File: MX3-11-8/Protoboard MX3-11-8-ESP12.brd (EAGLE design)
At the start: 74.4 x 99.4 mm, 638 parts, among them J1 DCJ0202, X1 ESP-12E, X3 RJ45

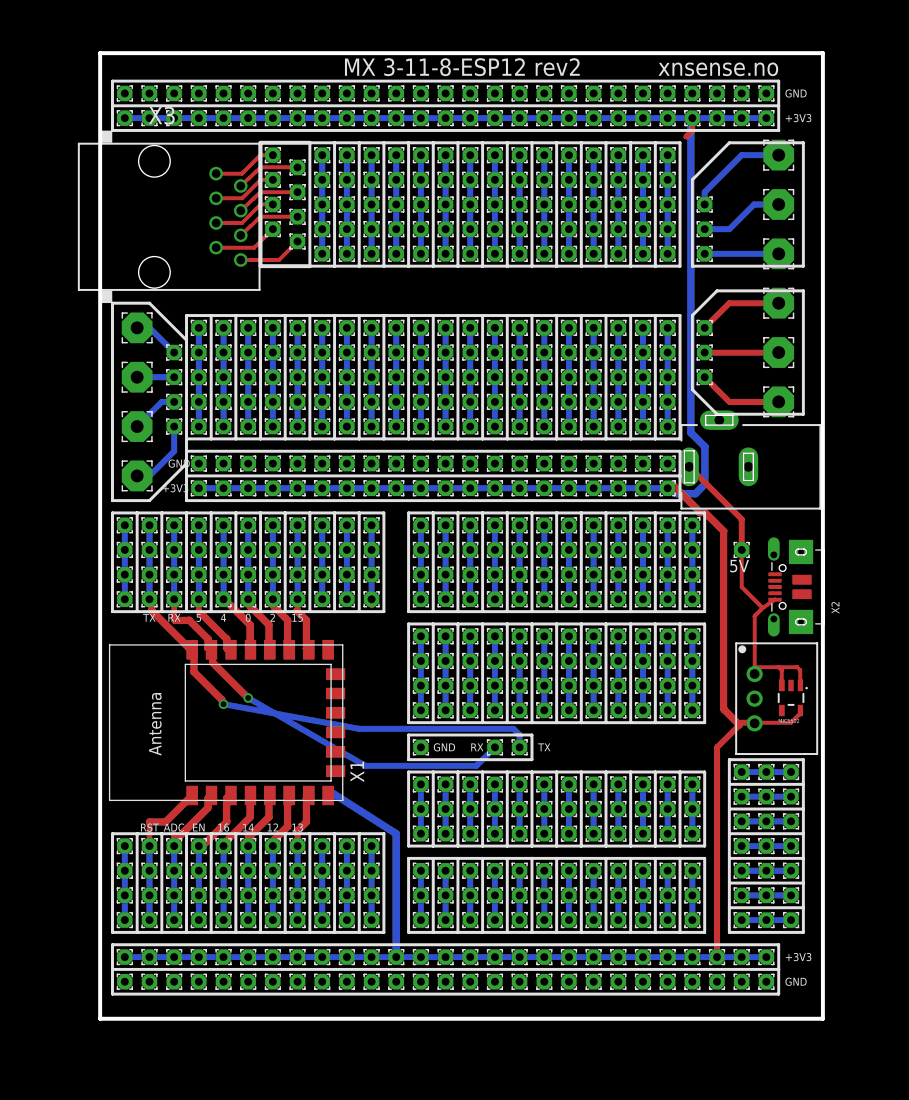
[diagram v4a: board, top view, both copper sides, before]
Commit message: Routed and Gerb files
Routed and produced gerb files
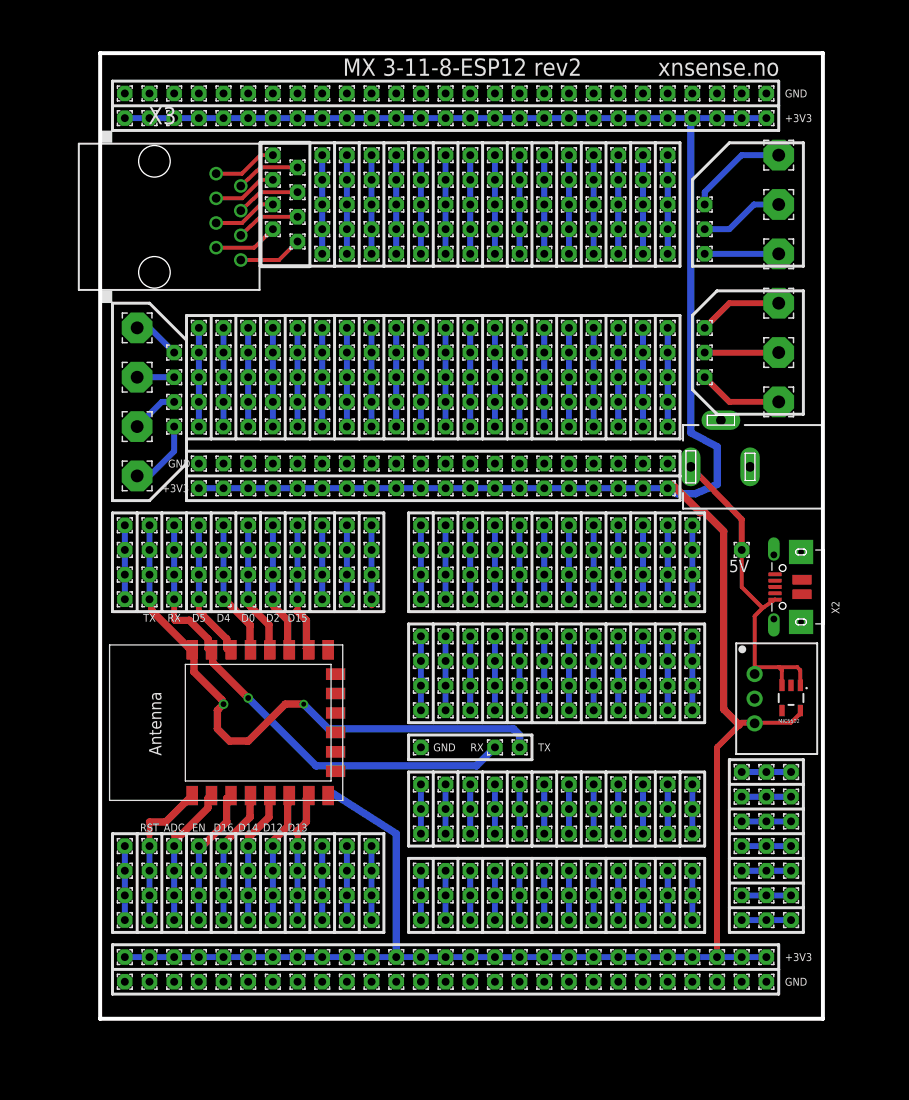
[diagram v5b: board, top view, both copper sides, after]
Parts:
- moved J1 0.16 mm to (63.9, 56.8)
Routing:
- net TX: track 54.5 -> 60.9 mm, vias 1 -> 2
- net RX: track 50.3 -> 51.3 mm
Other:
- board text added: "D0"
- board text added: "D12"
- board text added: "D13"
- board text added: "D14"
- board text added: "D15"
- board text added: "D16"
- board text added: "D2"
- board text added: "D4"
- board text added: "D5"
- board text removed: "0"
- board text removed: "12"
- board text removed: "13"
- board text removed: "14"
- board text removed: "15"
- board text removed: "16"
- board text removed: "2"
- board text removed: "4"
- board text removed: "5"
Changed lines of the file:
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@@
 <text x="7.62" y="19.685" size="0.8128" layer="25" align="center">ADC</text>
 <text x="10.16" y="19.685" size="0.8128" layer="25" align="center">EN</text>
-<text x="12.7" y="19.685" size="0.8128" layer="25" align="center">16</text>
-<text x="15.24" y="19.685" size="0.8128" layer="25" align="center">14</text>
-<text x="17.78" y="19.685" size="0.8128" layer="25" align="center">12</text>
-<text x="20.32" y="19.685" size="0.8128" layer="25" align="center">13</text>
+<text x="12.7" y="19.685" size="0.8128" layer="25" align="center">D16</text>
+<text x="15.24" y="19.685" size="0.8128" layer="25" align="center">D14</text>
+<text x="17.78" y="19.685" size="0.8128" layer="25" align="center">D12</text>
+<text x="20.32" y="19.685" size="0.8128" layer="25" align="center">D13</text>
 <text x="22.86" y="19.685" size="0.8128" layer="25" align="center"></text>
 <text x="25.4" y="19.685" size="0.8128" layer="25" align="center"></text>
@@
 <text x="25.4" y="41.275" size="0.8128" layer="25" align="center"></text>
 <text x="22.86" y="41.275" size="0.8128" layer="25" align="center"></text>
-<text x="20.32" y="41.275" size="0.8128" layer="25" align="center">15</text>
-<text x="17.78" y="41.275" size="0.8128" layer="25" align="center">2</text>
-<text x="15.24" y="41.275" size="0.8128" layer="25" align="center">0</text>
-<text x="12.7" y="41.275" size="0.8128" layer="25" align="center">4</text>
-<text x="10.16" y="41.275" size="0.8128" layer="25" align="center">5</text>
+<text x="20.32" y="41.275" size="0.8128" layer="25" align="center">D15</text>
+<text x="17.78" y="41.275" size="0.8128" layer="25" align="center">D2</text>
+<text x="15.24" y="41.275" size="0.8128" layer="25" align="center">D0</text>
+<text x="12.7" y="41.275" size="0.8128" layer="25" align="center">D4</text>
+<text x="10.16" y="41.275" size="0.8128" layer="25" align="center">D5</text>
 <text x="7.62" y="41.275" size="0.8128" layer="25" align="center">RX</text>
 <text x="5.08" y="41.275" size="0.8128" layer="25" align="center">TX</text>
@@
 <attribute name="VALUE" x="17.78" y="6.95" size="0.0254" layer="27"/>
 </element>
-<element name="J1" library="con-jack" package="DCJ0202" value="DCJ0202" x="63.735" y="56.815" smashed="yes" rot="R90">
-<attribute name="MPN" value="" x="63.735" y="56.815" size="1.778" layer="27" rot="R90" display="off"/>
-<attribute name="OC_NEWARK" value="unknown" x="63.735" y="56.815" size="1.778" layer="27" rot="R90" display="off"/>
-<attribute name="MF" value="" x="63.735" y="56.815" size="1.778" layer="27" rot="R90" display="off"/>
-<attribute name="OC_FARNELL" value="unknown" x="63.735" y="56.815" size="1.778" layer="27" rot="R90" display="off"/>
+<element name="J1" library="con-jack" package="DCJ0202" value="DCJ0202" x="63.9" y="56.815" smashed="yes" rot="R90">
+<attribute name="MPN" value="" x="63.9" y="56.815" size="1.778" layer="27" rot="R90" display="off"/>
+<attribute name="OC_NEWARK" value="unknown" x="63.9" y="56.815" size="1.778" layer="27" rot="R90" display="off"/>
+<attribute name="MF" value="" x="63.9" y="56.815" size="1.778" layer="27" rot="R90" display="off"/>
+<attribute name="OC_FARNELL" value="unknown" x="63.9" y="56.815" size="1.778" layer="27" rot="R90" display="off"/>
 </element>
 <element name="DC" library="dc-dc-converter" package="SIP3" value="R-78C1.8-1.0" x="67.37" y="32.95" smashed="yes" rot="R270"/>
@@
 <attribute name="VALUE" x="7.62" y="64.1" size="0.0254" layer="27"/>
 </element>
-<element name="X1" library="microbuilder" package="ESP-12E" value="ESP-12E" x="15.24" y="30.48" rot="R90"/>
+<element name="X1" library="microbuilder" package="ESP-12E" value="ESP-12E" x="15.24" y="30.48" smashed="yes" rot="R90"/>
 </elements>
 <signals>
@@
 <wire x1="66.04" y1="44.45" x2="68.2075" y2="42.2825" width="0.4064" layer="1"/>
 <wire x1="66.04" y1="48.26" x2="66.04" y2="51.41" width="0.6096" layer="1"/>
-<wire x1="66.04" y1="51.41" x2="60.635" y2="56.815" width="0.6096" layer="1"/>
+<wire x1="66.04" y1="51.41" x2="60.8" y2="56.815" width="0.6096" layer="1"/>
 </signal>
 <signal name="VDD">
@@
 <wire x1="61.7728" y1="52.07" x2="61.595" y2="52.07" width="0.6096" layer="1"/>
 <wire x1="59.055" y1="54.61" x2="58.42" y2="54.61" width="0.6096" layer="1"/>
-<wire x1="60.96" y1="92.71" x2="60.96" y2="91.44" width="0.6096" layer="1"/>
-<wire x1="60.96" y1="91.44" x2="60.325" y2="90.805" width="0.6096" layer="1"/>
 <wire x1="58.42" y1="54.61" x2="55.9816" y2="54.61" width="0.6096" layer="16"/>
 <wire x1="55.9816" y1="54.61" x2="55.88" y2="54.61" width="0.6096" layer="16"/>
@@
 <wire x1="62.2554" y1="52.1208" x2="62.23" y2="52.07" width="0.762" layer="1"/>
 <wire x1="60.8076" y1="60.325" x2="60.8076" y2="92.6592" width="0.762" layer="16"/>
-<wire x1="62.2554" y1="58.8772" x2="60.8076" y2="60.325" width="0.762" layer="16"/>
-<wire x1="62.2554" y1="55.0164" x2="62.2554" y2="58.8772" width="0.762" layer="16"/>
-<wire x1="61.2902" y1="54.0512" x2="62.2554" y2="55.0164" width="0.762" layer="16"/>
+<wire x1="63.5254" y1="58.8772" x2="60.8076" y2="60.325" width="0.762" layer="16"/>
+<wire x1="63.5254" y1="55.0164" x2="63.5254" y2="58.8772" width="0.762" layer="16"/>
+<wire x1="61.2902" y1="54.0512" x2="63.5254" y2="55.0164" width="0.762" layer="16"/>
 <wire x1="59.3598" y1="54.0512" x2="61.2902" y2="54.0512" width="0.762" layer="16"/>
 <wire x1="58.8772" y1="54.5338" x2="59.3598" y2="54.0512" width="0.762" layer="16"/>
@@
 <wire x1="5.08" y1="45.847" x2="5.08" y2="45.72" width="0.6096" layer="16"/>
 <wire x1="5.08" y1="45.72" x2="5.08" y2="43.18" width="0.6096" layer="16"/>
-<wire x1="43.18" y1="27.94" x2="43.18" y2="29.21" width="0.6096" layer="16"/>
-<wire x1="43.18" y1="29.21" x2="42.545" y2="29.845" width="0.6096" layer="16"/>
-<wire x1="42.545" y1="29.845" x2="26.67" y2="29.845" width="0.6096" layer="16"/>
-<wire x1="26.67" y1="29.845" x2="12.7" y2="32.385" width="0.6096" layer="16"/>
 <via x="12.7" y="32.385" extent="1-16" drill="0.6"/>
 <contactref element="X1" pad="16"/>
@@
 <wire x1="5.3086" y1="42.9514" x2="5.08" y2="43.18" width="0.762" layer="1"/>
 <wire x1="9.1694" y1="38.1254" x2="9.47" y2="37.98" width="0.762" layer="1"/>
+<wire x1="43.18" y1="27.94" x2="43.18" y2="29.21" width="0.762" layer="16"/>
+<wire x1="43.18" y1="29.21" x2="42.545" y2="29.845" width="0.762" layer="16"/>
+<wire x1="42.545" y1="29.845" x2="23.495" y2="29.845" width="0.762" layer="16"/>
+<wire x1="23.495" y1="29.845" x2="20.955" y2="32.385" width="0.762" layer="16"/>
+<via x="20.955" y="32.385" extent="1-16" drill="0.508"/>
+<wire x1="20.955" y1="32.385" x2="19.05" y2="32.385" width="0.762" layer="1"/>
+<wire x1="19.05" y1="32.385" x2="15.24" y2="28.575" width="0.762" layer="1"/>
+<wire x1="15.24" y1="28.575" x2="13.335" y2="28.575" width="0.762" layer="1"/>
+<wire x1="13.335" y1="28.575" x2="12.065" y2="29.845" width="0.762" layer="1"/>
+<wire x1="12.065" y1="29.845" x2="12.065" y2="31.75" width="0.762" layer="1"/>
+<wire x1="12.065" y1="31.75" x2="12.7" y2="32.385" width="0.762" layer="1"/>
 </signal>
 <signal name="RX">
@@
 <wire x1="7.62" y1="45.847" x2="7.62" y2="45.72" width="0.6096" layer="16"/>
 <wire x1="7.62" y1="45.72" x2="7.62" y2="43.18" width="0.6096" layer="16"/>
-<wire x1="40.64" y1="27.94" x2="38.735" y2="26.035" width="0.6096" layer="16"/>
-<wire x1="38.735" y1="26.035" x2="27.305" y2="26.035" width="0.6096" layer="16"/>
-<wire x1="27.305" y1="26.035" x2="15.24" y2="33.02" width="0.6096" layer="16"/>
 <via x="15.24" y="33.02" extent="1-16" drill="0.6"/>
 <wire x1="7.62" y1="43.18" x2="7.62" y2="41.275" width="0.6096" layer="1"/>
@@
 <wire x1="15.24" y1="33.02" x2="11.5824" y2="36.6776" width="0.762" layer="1"/>
 <wire x1="11.5824" y1="37.6428" x2="11.47" y2="37.98" width="0.762" layer="1"/>
+<wire x1="40.64" y1="27.94" x2="38.735" y2="26.035" width="0.762" layer="16"/>
+<wire x1="38.735" y1="26.035" x2="22.225" y2="26.035" width="0.762" layer="16"/>
+<wire x1="22.225" y1="26.035" x2="15.24" y2="33.02" width="0.762" layer="16"/>
 </signal>
 <signal name="N$113">

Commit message: Silkscreen text fixes
Silkscreen text fixes
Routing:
- net TX: track 60.9 -> 55.4 mm
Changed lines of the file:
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@@
 <wire x1="5.08" y1="45.847" x2="5.08" y2="45.72" width="0.6096" layer="16"/>
 <wire x1="5.08" y1="45.72" x2="5.08" y2="43.18" width="0.6096" layer="16"/>
-<via x="12.7" y="32.385" extent="1-16" drill="0.6"/>
 <contactref element="X1" pad="16"/>
 <wire x1="5.3086" y1="45.847" x2="5.08" y2="45.72" width="0.762" layer="16"/>
 <wire x1="5.3086" y1="45.847" x2="5.08" y2="45.847" width="0.762" layer="16"/>
 <wire x1="5.3086" y1="48.26" x2="5.08" y2="48.26" width="0.762" layer="16"/>
-<wire x1="9.652" y1="35.7124" x2="9.652" y2="37.6428" width="0.762" layer="1"/>
-<wire x1="12.5476" y1="32.8168" x2="9.652" y2="35.7124" width="0.762" layer="1"/>
-<wire x1="9.652" y1="37.6428" x2="9.47" y2="37.98" width="0.762" layer="1"/>
-<wire x1="12.5476" y1="32.8168" x2="12.7" y2="32.385" width="0.762" layer="1"/>
 <wire x1="5.3086" y1="41.9862" x2="5.3086" y2="42.9514" width="0.762" layer="1"/>
 <wire x1="9.1694" y1="38.1254" x2="5.3086" y2="41.9862" width="0.762" layer="1"/>
 <wire x1="5.3086" y1="42.9514" x2="5.08" y2="43.18" width="0.762" layer="1"/>
 <wire x1="9.1694" y1="38.1254" x2="9.47" y2="37.98" width="0.762" layer="1"/>
-<wire x1="43.18" y1="27.94" x2="43.18" y2="29.21" width="0.762" layer="16"/>
-<wire x1="43.18" y1="29.21" x2="42.545" y2="29.845" width="0.762" layer="16"/>
-<wire x1="42.545" y1="29.845" x2="23.495" y2="29.845" width="0.762" layer="16"/>
-<wire x1="23.495" y1="29.845" x2="20.955" y2="32.385" width="0.762" layer="16"/>
-<via x="20.955" y="32.385" extent="1-16" drill="0.508"/>
-<wire x1="20.955" y1="32.385" x2="19.05" y2="32.385" width="0.762" layer="1"/>
-<wire x1="19.05" y1="32.385" x2="15.24" y2="28.575" width="0.762" layer="1"/>
-<wire x1="15.24" y1="28.575" x2="13.335" y2="28.575" width="0.762" layer="1"/>
-<wire x1="13.335" y1="28.575" x2="12.065" y2="29.845" width="0.762" layer="1"/>
-<wire x1="12.065" y1="29.845" x2="12.065" y2="31.75" width="0.762" layer="1"/>
-<wire x1="12.065" y1="31.75" x2="12.7" y2="32.385" width="0.762" layer="1"/>
+<wire x1="43.18" y1="27.94" x2="43.18" y2="28.575" width="0.762" layer="1"/>
+<wire x1="43.18" y1="28.575" x2="41.91" y2="29.845" width="0.762" layer="1"/>
+<wire x1="41.91" y1="29.845" x2="29.21" y2="29.845" width="0.762" layer="1"/>
+<via x="29.21" y="29.845" extent="1-16" drill="0.508"/>
+<wire x1="29.21" y1="29.845" x2="14.605" y2="29.845" width="0.762" layer="16"/>
+<wire x1="14.605" y1="29.845" x2="11.43" y2="33.02" width="0.762" layer="16"/>
+<via x="11.43" y="33.02" extent="1-16" drill="0.508"/>
+<wire x1="11.43" y1="33.02" x2="9.525" y2="34.925" width="0.762" layer="1"/>
+<wire x1="9.525" y1="34.925" x2="9.525" y2="37.925" width="0.762" layer="1"/>
+<wire x1="9.525" y1="37.925" x2="9.47" y2="37.98" width="0.762" layer="1"/>
 </signal>
 <signal name="RX">
